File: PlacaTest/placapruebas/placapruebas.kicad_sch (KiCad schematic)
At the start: 9 parts, among them SW3 SW_Push, SW4 SW_Push

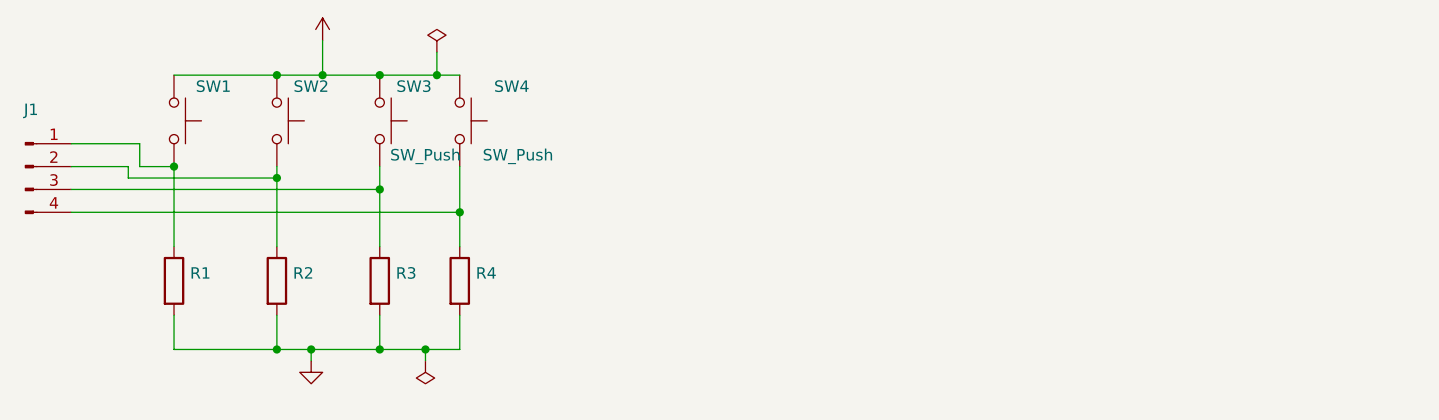
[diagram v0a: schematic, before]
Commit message: Agrego circuito de pulsador y de leds
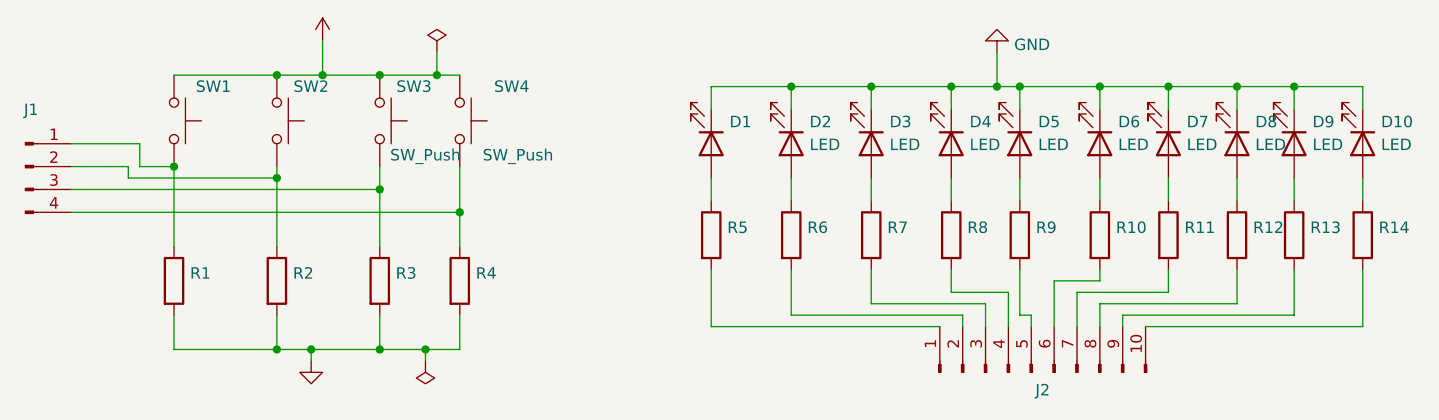
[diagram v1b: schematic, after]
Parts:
- added D1: (no value), symbol Device:LED
- added D10, D2, D3, D4, D5, D6, D7, D8, D9: LED, symbol Device:LED
- added J2: (no value), symbol Connector:Conn_01x10_Male
- added R10, R11, R12, R13, R14, R5, R6, R7, R8, R9: (no value), symbol Device:R
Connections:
- net GND: now also D1.1 (K), D10.1 (K), D2.1 (K), D3.1 (K), D4.1 (K), D5.1 (K), D6.1 (K), D7.1 (K), D8.1 (K), D9.1 (K)
- new net: D1.2 (A), R5.1
- new net: D6.2 (A), R10.1
- new net: D5.2 (A), R9.1
- new net: J2.5 (Pin_5), R9.2
- new net: D10.2 (A), R14.1
- new net: D4.2 (A), R8.1
- new net: J2.4 (Pin_4), R8.2
- new net: D3.2 (A), R7.1
- new net: J2.3 (Pin_3), R7.2
- new net: D8.2 (A), R12.1
- new net: J2.8 (Pin_8), R12.2
- new net: J2.6 (Pin_6), R10.2
- new net: D9.2 (A), R13.1
- new net: J2.9 (Pin_9), R13.2
- new net: J2.1 (Pin_1), R5.2
- new net: D7.2 (A), R11.1
- new net: D2.2 (A), R6.1
- new net: J2.10 (Pin_10), R14.2
- new net: J2.2 (Pin_2), R6.2
- new net: J2.7 (Pin_7), R11.2
